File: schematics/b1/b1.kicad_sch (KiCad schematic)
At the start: 0 parts

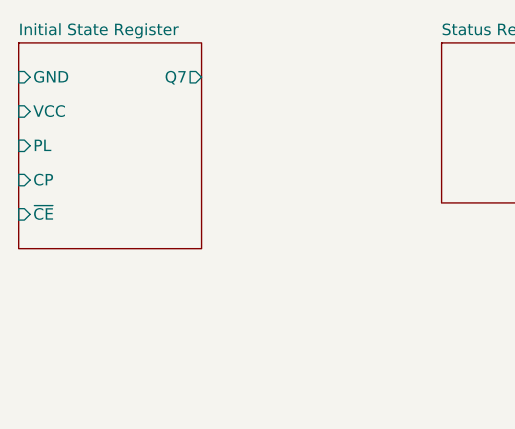
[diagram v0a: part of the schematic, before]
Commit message: Changed GND hierarchical labels to global.
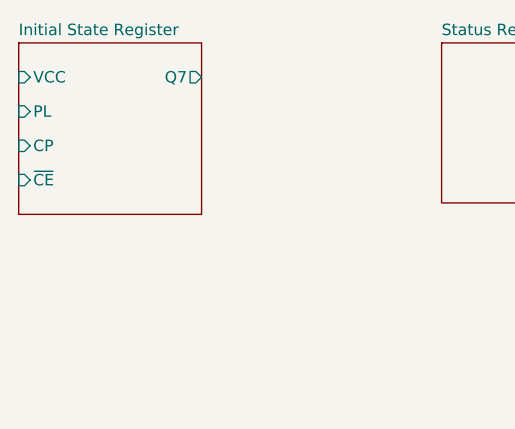
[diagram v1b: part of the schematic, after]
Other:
- sheet Initial State Register ports: added none; removed GND
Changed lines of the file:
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@@
     (comment 4 "A B1 (Badger One) node is the core hardware unit of the Badger sytem. It handles card")
   )
-  (sheet (at 44.45 34.29) (size 20.32 22.86) (fields_autoplaced)
+  (sheet (at 44.45 34.29) (size 20.32 19.05) (fields_autoplaced)
     (stroke (width 0.1524) (type solid))
     (fill (color 0 0 0 0.0000))
@@
       (effects (font (size 1.27 1.27)) (justify left bottom))
     )
-    (property "Sheetfile" "initial_state.kicad_sch" (at 44.45 57.7346 0)
+    (property "Sheetfile" "initial_state.kicad_sch" (at 44.45 53.9246 0)
       (effects (font (size 1.27 1.27)) (justify left top) hide)
     )
-    (pin "GND" input (at 44.45 38.1 180)
+    (pin "PL" input (at 44.45 41.91 180)
       (effects (font (size 1.27 1.27)) (justify left))
     )
-    (pin "VCC" input (at 44.45 41.91 180)
+    (pin "CP" input (at 44.45 45.72 180)
       (effects (font (size 1.27 1.27)) (justify left))
     )
-    (pin "PL" input (at 44.45 45.72 180)
-      (effects (font (size 1.27 1.27)) (justify left))
-    )
-    (pin "CP" input (at 44.45 49.53 180)
-      (effects (font (size 1.27 1.27)) (justify left))
-    )
-    (pin "~{CE}" input (at 44.45 53.34 180)
+    (pin "~{CE}" input (at 44.45 49.53 180)
       (effects (font (size 1.27 1.27)) (justify left))
     )
@@
       (effects (font (size 1.27 1.27)) (justify right))
     )
+    (pin "VCC" input (at 44.45 38.1 180)
+      (effects (font (size 1.27 1.27)) (justify left))
+    )
     (instances

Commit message: Added schematic page for the status block.
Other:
- sheet Status Register renamed Status Block
- sheet Initial State Register: file initial_state.kicad_sch -> initial_state_register.kicad_sch
- sheet Status Block: file status.kicad_sch -> status_block.kicad_sch
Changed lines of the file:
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@@
   (title_block
     (title "B1")
-    (date "2024-02-01")
+    (date "2024-02-05")
     (rev "1")
     (company "shawnd.xyz")
@@
       (effects (font (size 1.27 1.27)) (justify left bottom))
     )
-    (property "Sheetfile" "initial_state.kicad_sch" (at 44.45 53.9246 0)
+    (property "Sheetfile" "initial_state_register.kicad_sch" (at 44.45 53.9246 0)
       (effects (font (size 1.27 1.27)) (justify left top) hide)
     )
@@
     )
   )
-  (sheet (at 91.44 34.29) (size 19.05 17.78) (fields_autoplaced)
+  (sheet (at 44.45 58.42) (size 20.32 17.78) (fields_autoplaced)
     (stroke (width 0.1524) (type solid))
     (fill (color 0 0 0 0.0000))
-    (property "Sheetname" "Status Register" (at 91.44 33.5784 0)
+    (property "Sheetname" "Status Block" (at 44.45 57.7084 0)
       (effects (font (size 1.27 1.27)) (justify left bottom))
     )
-    (property "Sheetfile" "status.kicad_sch" (at 91.44 52.6546 0)
+    (property "Sheetfile" "status_block.kicad_sch" (at 44.45 76.7846 0)
       (effects (font (size 1.27 1.27)) (justify left top) hide)
     )

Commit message: Added status block to the index page.
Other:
- sheet Status Block ports: added BUZZ, RCLK, SER, SRCLK, VCC; removed none
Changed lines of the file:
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@@
     (comment 4 "A B1 (Badger One) node is the core hardware unit of the Badger sytem. It handles card")
   )
-  (sheet (at 44.45 34.29) (size 20.32 19.05) (fields_autoplaced)
+  (sheet (at 49.53 33.02) (size 20.32 19.05) (fields_autoplaced)
     (stroke (width 0.1524) (type solid))
     (fill (color 0 0 0 0.0000))
-    (property "Sheetname" "Initial State Register" (at 44.45 33.5784 0)
+    (property "Sheetname" "Initial State Register" (at 49.53 32.3084 0)
       (effects (font (size 1.27 1.27)) (justify left bottom))
     )
-    (property "Sheetfile" "initial_state_register.kicad_sch" (at 44.45 53.9246 0)
+    (property "Sheetfile" "initial_state_register.kicad_sch" (at 49.53 52.6546 0)
       (effects (font (size 1.27 1.27)) (justify left top) hide)
     )
-    (pin "PL" input (at 44.45 41.91 180)
+    (pin "PL" input (at 49.53 40.64 180)
       (effects (font (size 1.27 1.27)) (justify left))
     )
-    (pin "CP" input (at 44.45 45.72 180)
+    (pin "CP" input (at 49.53 44.45 180)
       (effects (font (size 1.27 1.27)) (justify left))
     )
-    (pin "~{CE}" input (at 44.45 49.53 180)
+    (pin "~{CE}" input (at 49.53 48.26 180)
       (effects (font (size 1.27 1.27)) (justify left))
     )
-    (pin "Q7" output (at 64.77 38.1 0)
+    (pin "Q7" output (at 69.85 36.83 0)
       (effects (font (size 1.27 1.27)) (justify right))
     )
-    (pin "VCC" input (at 44.45 38.1 180)
+    (pin "VCC" input (at 49.53 36.83 180)
       (effects (font (size 1.27 1.27)) (justify left))
     )
@@
     )
   )
-  (sheet (at 44.45 58.42) (size 20.32 17.78) (fields_autoplaced)
+  (sheet (at 49.53 57.15) (size 20.32 22.86) (fields_autoplaced)
     (stroke (width 0.1524) (type solid))
     (fill (color 0 0 0 0.0000))
-    (property "Sheetname" "Status Block" (at 44.45 57.7084 0)
+    (property "Sheetname" "Status Block" (at 49.53 56.4384 0)
       (effects (font (size 1.27 1.27)) (justify left bottom))
     )
-    (property "Sheetfile" "status_block.kicad_sch" (at 44.45 76.7846 0)
+    (property "Sheetfile" "status_block.kicad_sch" (at 49.53 80.5946 0)
       (effects (font (size 1.27 1.27)) (justify left top) hide)
     )
+    (pin "VCC" input (at 49.53 60.96 180)
+      (effects (font (size 1.27 1.27)) (justify left))
+    )
+    (pin "BUZZ" input (at 49.53 76.2 180)
+      (effects (font (size 1.27 1.27)) (justify left))
+    )
+    (pin "RCLK" input (at 49.53 64.77 180)
+      (effects (font (size 1.27 1.27)) (justify left))
+    )
+    (pin "SER" input (at 49.53 68.58 180)
+      (effects (font (size 1.27 1.27)) (justify left))
+    )
+    (pin "SRCLK" input (at 49.53 72.39 180)
+      (effects (font (size 1.27 1.27)) (justify left))
+    )
     (instances

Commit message: Added schematic page for scanner.
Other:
- sheet Scanner ports: added MISO, MOSI, RST, SCK, SDA, VCC; removed none
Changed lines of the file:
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@@
     )
   )
-  (sheet (at 166.37 101.6) (size 12.7 17.78) (fields_autoplaced)
+  (sheet (at 49.53 85.09) (size 20.32 22.86) (fields_autoplaced)
     (stroke (width 0.1524) (type solid))
     (fill (color 0 0 0 0.0000))
-    (property "Sheetname" "Scanner" (at 166.37 100.8884 0)
+    (property "Sheetname" "Scanner" (at 49.53 84.3784 0)
       (effects (font (size 1.27 1.27)) (justify left bottom))
     )
-    (property "Sheetfile" "scanner.kicad_sch" (at 166.37 119.9646 0)
+    (property "Sheetfile" "scanner.kicad_sch" (at 49.53 108.5346 0)
       (effects (font (size 1.27 1.27)) (justify left top) hide)
     )
+    (pin "MISO" output (at 69.85 88.9 0)
+      (effects (font (size 1.27 1.27)) (justify right))
+    )
+    (pin "VCC" input (at 49.53 88.9 180)
+      (effects (font (size 1.27 1.27)) (justify left))
+    )
+    (pin "SDA" input (at 49.53 92.71 180)
+      (effects (font (size 1.27 1.27)) (justify left))
+    )
+    (pin "SCK" input (at 49.53 96.52 180)
+      (effects (font (size 1.27 1.27)) (justify left))
+    )
+    (pin "MOSI" input (at 49.53 100.33 180)
+      (effects (font (size 1.27 1.27)) (justify left))
+    )
+    (pin "RST" input (at 49.53 104.14 180)
+      (effects (font (size 1.27 1.27)) (justify left))
+    )
     (instances

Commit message: Added scanner pins to the index.
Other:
- sheet LoRa ports: added DIO0, MISO, MOSI, NSS, RST, SCK; removed none
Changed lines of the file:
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@@
     (comment 4 "A B1 (Badger One) node is the core hardware unit of the Badger sytem. It handles card")
   )
-  (sheet (at 49.53 33.02) (size 20.32 19.05) (fields_autoplaced)
+  (sheet (at 78.74 29.21) (size 20.32 19.05) (fields_autoplaced)
     (stroke (width 0.1524) (type solid))
     (fill (color 0 0 0 0.0000))
-    (property "Sheetname" "Initial State Register" (at 49.53 32.3084 0)
+    (property "Sheetname" "Initial State Register" (at 78.74 28.4984 0)
       (effects (font (size 1.27 1.27)) (justify left bottom))
     )
-    (property "Sheetfile" "initial_state_register.kicad_sch" (at 49.53 52.6546 0)
+    (property "Sheetfile" "initial_state_register.kicad_sch" (at 78.74 48.8446 0)
       (effects (font (size 1.27 1.27)) (justify left top) hide)
     )
-    (pin "PL" input (at 49.53 40.64 180)
+    (pin "PL" input (at 78.74 36.83 180)
       (effects (font (size 1.27 1.27)) (justify left))
     )
-    (pin "CP" input (at 49.53 44.45 180)
+    (pin "CP" input (at 78.74 40.64 180)
       (effects (font (size 1.27 1.27)) (justify left))
     )
-    (pin "~{CE}" input (at 49.53 48.26 180)
+    (pin "~{CE}" input (at 78.74 44.45 180)
       (effects (font (size 1.27 1.27)) (justify left))
     )
-    (pin "Q7" output (at 69.85 36.83 0)
+    (pin "Q7" output (at 99.06 33.02 0)
       (effects (font (size 1.27 1.27)) (justify right))
     )
-    (pin "VCC" input (at 49.53 36.83 180)
+    (pin "VCC" input (at 78.74 33.02 180)
       (effects (font (size 1.27 1.27)) (justify left))
     )
@@
     )
   )
-  (sheet (at 49.53 85.09) (size 20.32 22.86) (fields_autoplaced)
+  (sheet (at 78.74 81.28) (size 20.32 22.86) (fields_autoplaced)
     (stroke (width 0.1524) (type solid))
     (fill (color 0 0 0 0.0000))
-    (property "Sheetname" "Scanner" (at 49.53 84.3784 0)
+    (property "Sheetname" "Scanner" (at 78.74 80.5684 0)
       (effects (font (size 1.27 1.27)) (justify left bottom))
     )
-    (property "Sheetfile" "scanner.kicad_sch" (at 49.53 108.5346 0)
+    (property "Sheetfile" "scanner.kicad_sch" (at 78.74 104.7246 0)
       (effects (font (size 1.27 1.27)) (justify left top) hide)
     )
-    (pin "MISO" output (at 69.85 88.9 0)
+    (pin "MISO" output (at 99.06 85.09 0)
       (effects (font (size 1.27 1.27)) (justify right))
     )
-    (pin "VCC" input (at 49.53 88.9 180)
+    (pin "VCC" input (at 78.74 85.09 180)
       (effects (font (size 1.27 1.27)) (justify left))
     )
-    (pin "SDA" input (at 49.53 92.71 180)
+    (pin "SDA" input (at 78.74 88.9 180)
       (effects (font (size 1.27 1.27)) (justify left))
     )
-    (pin "SCK" input (at 49.53 96.52 180)
+    (pin "SCK" input (at 78.74 92.71 180)
       (effects (font (size 1.27 1.27)) (justify left))
     )
-    (pin "MOSI" input (at 49.53 100.33 180)
+    (pin "MOSI" input (at 78.74 96.52 180)
       (effects (font (size 1.27 1.27)) (justify left))
     )
-    (pin "RST" input (at 49.53 104.14 180)
+    (pin "RST" input (at 78.74 100.33 180)
       (effects (font (size 1.27 1.27)) (justify left))
     )
@@
     )
   )
-  (sheet (at 194.31 101.6) (size 22.86 17.78) (fields_autoplaced)
+  (sheet (at 78.74 107.95) (size 20.32 22.86) (fields_autoplaced)
     (stroke (width 0.1524) (type solid))
     (fill (color 0 0 0 0.0000))
-    (property "Sheetname" "LoRa" (at 194.31 100.8884 0)
+    (property "Sheetname" "LoRa" (at 78.74 107.2384 0)
       (effects (font (size 1.27 1.27)) (justify left bottom))
     )
-    (property "Sheetfile" "lora.kicad_sch" (at 194.31 119.9646 0)
+    (property "Sheetfile" "lora.kicad_sch" (at 78.74 131.3946 0)
       (effects (font (size 1.27 1.27)) (justify left top) hide)
+    )
+    (pin "DIO0" output (at 99.06 111.76 0)
+      (effects (font (size 1.27 1.27)) (justify right))
+    )
+    (pin "RST" input (at 78.74 111.76 180)
+      (effects (font (size 1.27 1.27)) (justify left))
+    )
+    (pin "MISO" input (at 78.74 115.57 180)
+      (effects (font (size 1.27 1.27)) (justify left))
+    )
+    (pin "SCK" input (at 78.74 119.38 180)
+      (effects (font (size 1.27 1.27)) (justify left))
+    )
+    (pin "NSS" input (at 78.74 123.19 180)
+      (effects (font (size 1.27 1.27)) (justify left))
+    )
+    (pin "MOSI" input (at 78.74 127 180)
+      (effects (font (size 1.27 1.27)) (justify left))
     )
     (instances
@@
     )
   )
-  (sheet (at 49.53 57.15) (size 20.32 22.86) (fields_autoplaced)
+  (sheet (at 78.74 53.34) (size 20.32 22.86) (fields_autoplaced)
     (stroke (width 0.1524) (type solid))
     (fill (color 0 0 0 0.0000))
-    (property "Sheetname" "Status Block" (at 49.53 56.4384 0)
+    (property "Sheetname" "Status Block" (at 78.74 52.6284 0)
       (effects (font (size 1.27 1.27)) (justify left bottom))
     )
-    (property "Sheetfile" "status_block.kicad_sch" (at 49.53 80.5946 0)
+    (property "Sheetfile" "status_block.kicad_sch" (at 78.74 76.7846 0)
       (effects (font (size 1.27 1.27)) (justify left top) hide)
     )
-    (pin "VCC" input (at 49.53 60.96 180)
+    (pin "VCC" input (at 78.74 57.15 180)
       (effects (font (size 1.27 1.27)) (justify left))
     )
-    (pin "BUZZ" input (at 49.53 76.2 180)
+    (pin "BUZZ" input (at 78.74 72.39 180)
       (effects (font (size 1.27 1.27)) (justify left))
     )
-    (pin "RCLK" input (at 49.53 64.77 180)
+    (pin "RCLK" input (at 78.74 60.96 180)
       (effects (font (size 1.27 1.27)) (justify left))
     )
-    (pin "SER" input (at 49.53 68.58 180)
+    (pin "SER" input (at 78.74 64.77 180)
       (effects (font (size 1.27 1.27)) (justify left))
     )
-    (pin "SRCLK" input (at 49.53 72.39 180)
+    (pin "SRCLK" input (at 78.74 68.58 180)
       (effects (font (size 1.27 1.27)) (justify left))
     )
